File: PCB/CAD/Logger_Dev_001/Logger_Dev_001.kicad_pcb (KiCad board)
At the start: 2 copper layers, 72 parts, among them J1 Conn_Coaxial, J3 Micro_SD_Card_Det1, J4 Connector, USB-TYPE-C-16P, Q1 BC847BS, Q2 MMBT3904, U1 L76-M33, U2 ESP32-C6-WROOM-1, U5 AMS1117, U6 CP2102-GMR

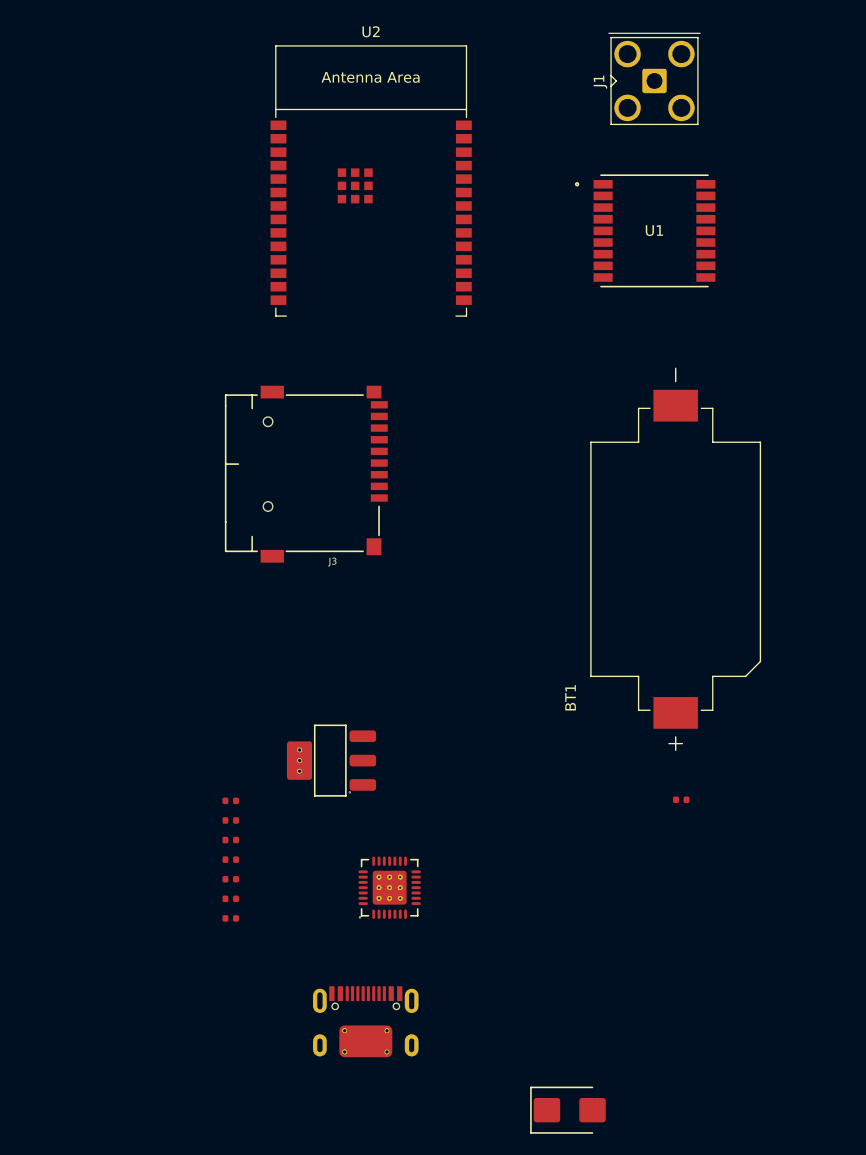
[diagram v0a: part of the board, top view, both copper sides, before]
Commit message: Update PCB
Added board outline, currently not showing in 3d viewer
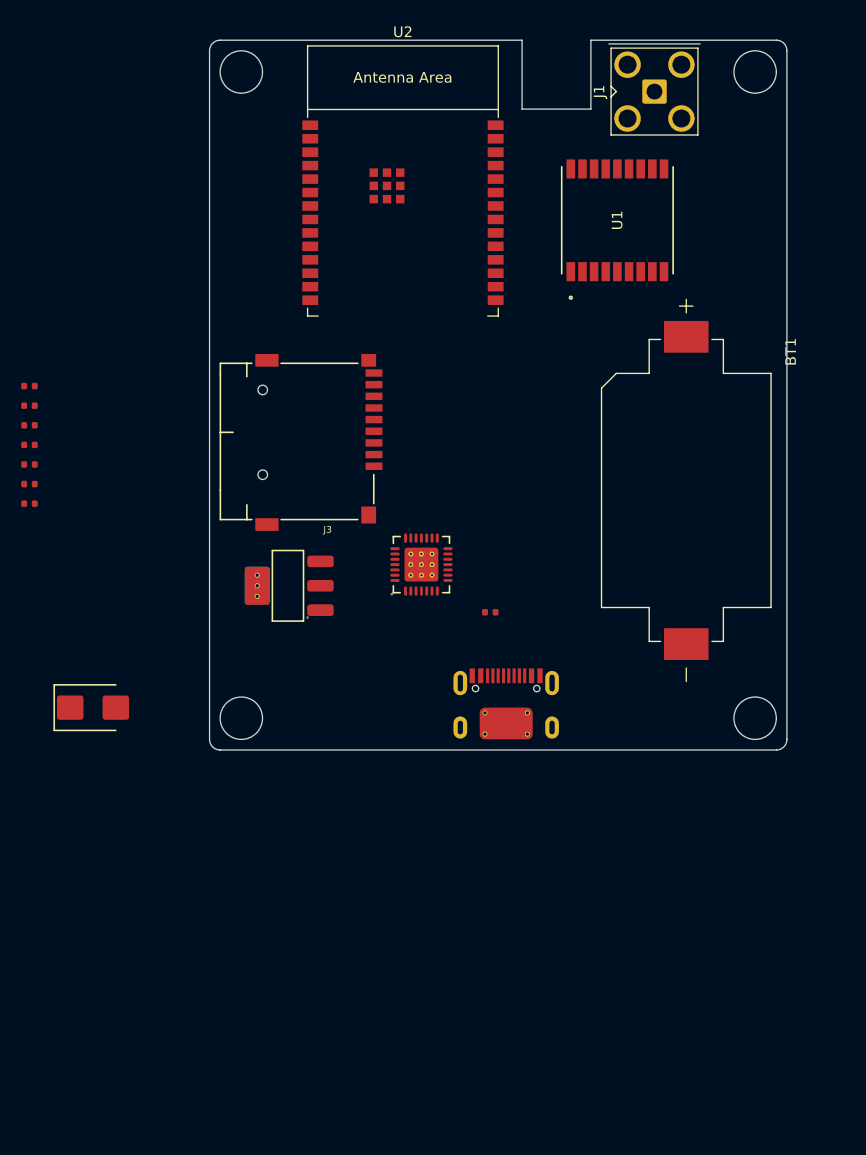
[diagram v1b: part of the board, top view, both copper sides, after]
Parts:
- moved D4 58.9 mm to (99.0, 107.0)
- moved C15 43.5 mm to (93.0, 78.5)
- moved R17 43.5 mm to (93.0, 80.3)
- moved R19 43.5 mm to (93.0, 84.0)
- moved R21 43.5 mm to (93.0, 87.8)
- moved C14 43.5 mm to (93.0, 76.7)
- moved R18 43.5 mm to (93.0, 82.2)
- moved R20 43.5 mm to (93.0, 85.9)
- moved J4 32.8 mm to (138.0, 106.5)
- moved U6 30.6 mm to (130.0, 93.5)
- moved C5 25.3 mm to (136.5, 98.0)
- moved U5 17.0 mm to (117.5, 95.5)
- moved BT1 6.58 mm to (155.0, 86.5), turned to -90 degrees
- moved U1 3.64 mm to (148.5, 61.0), turned to 90 degrees
- moved J3 3.04 mm to (118.5, 81.0)
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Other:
- board outline added: 54.5 x 67 mm

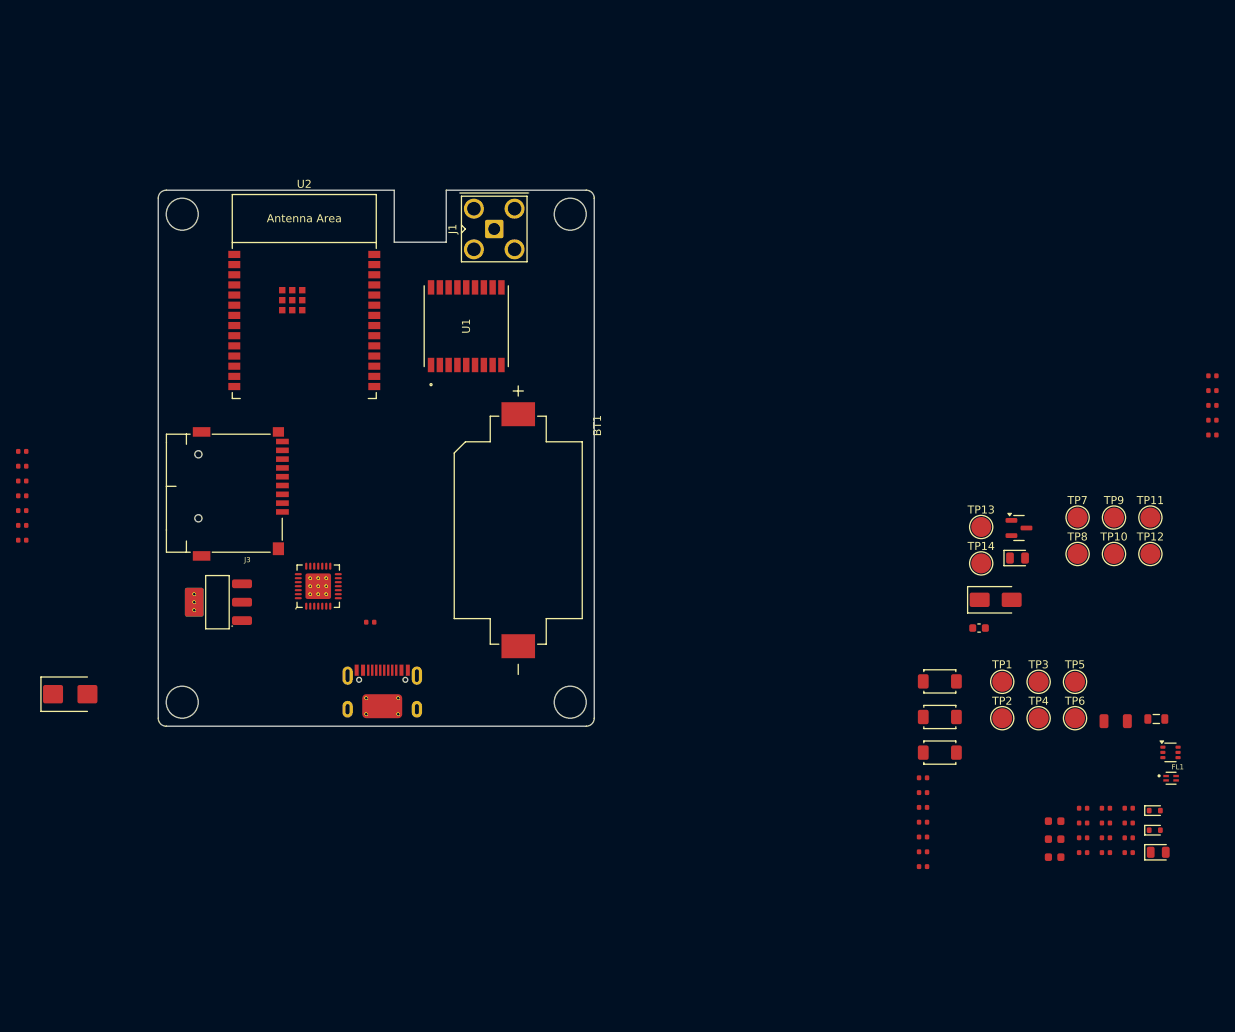
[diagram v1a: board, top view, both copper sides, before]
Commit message: PCB Board Update
Moved drill holes but board is broken by rf connector
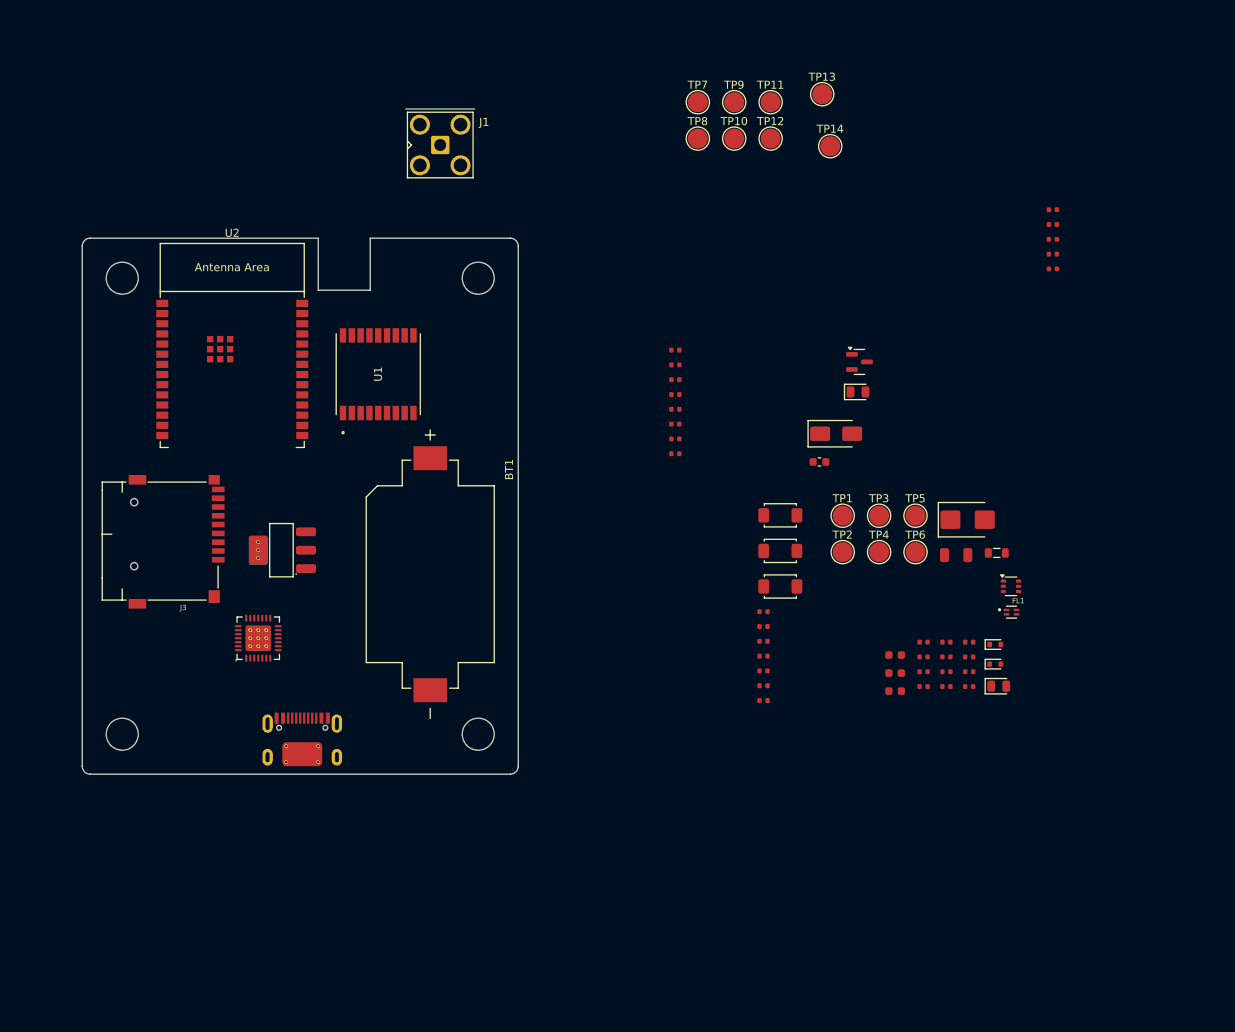
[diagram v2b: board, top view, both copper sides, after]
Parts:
- moved D4 114.3 mm to (211.2, 85.2)
- moved C14 82.4 mm to (174.6, 65.8)
- moved C15 82.4 mm to (174.6, 67.7)
- moved R17 82.4 mm to (174.6, 69.5)
- moved R18 82.4 mm to (174.6, 71.4)
- moved R19 82.4 mm to (174.6, 73.2)
- moved R20 82.4 mm to (174.6, 75.1)
- moved R21 82.4 mm to (174.6, 76.9)
- moved TP10 70.3 mm to (182.0, 37.5)
- moved TP11 70.3 mm to (186.6, 33.0)
- moved TP12 70.3 mm to (186.6, 37.5)
- moved TP7 70.3 mm to (177.4, 33.0)
- moved TP8 70.3 mm to (177.4, 37.5)
- moved TP9 70.3 mm to (182.0, 33.0)
- moved TP13 57.6 mm to (193.0, 32.0)
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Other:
- outline, holes or cut-outs redrawn

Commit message: PCB Layout Update
PCB Board Fixed
Most Components except Resistors placed
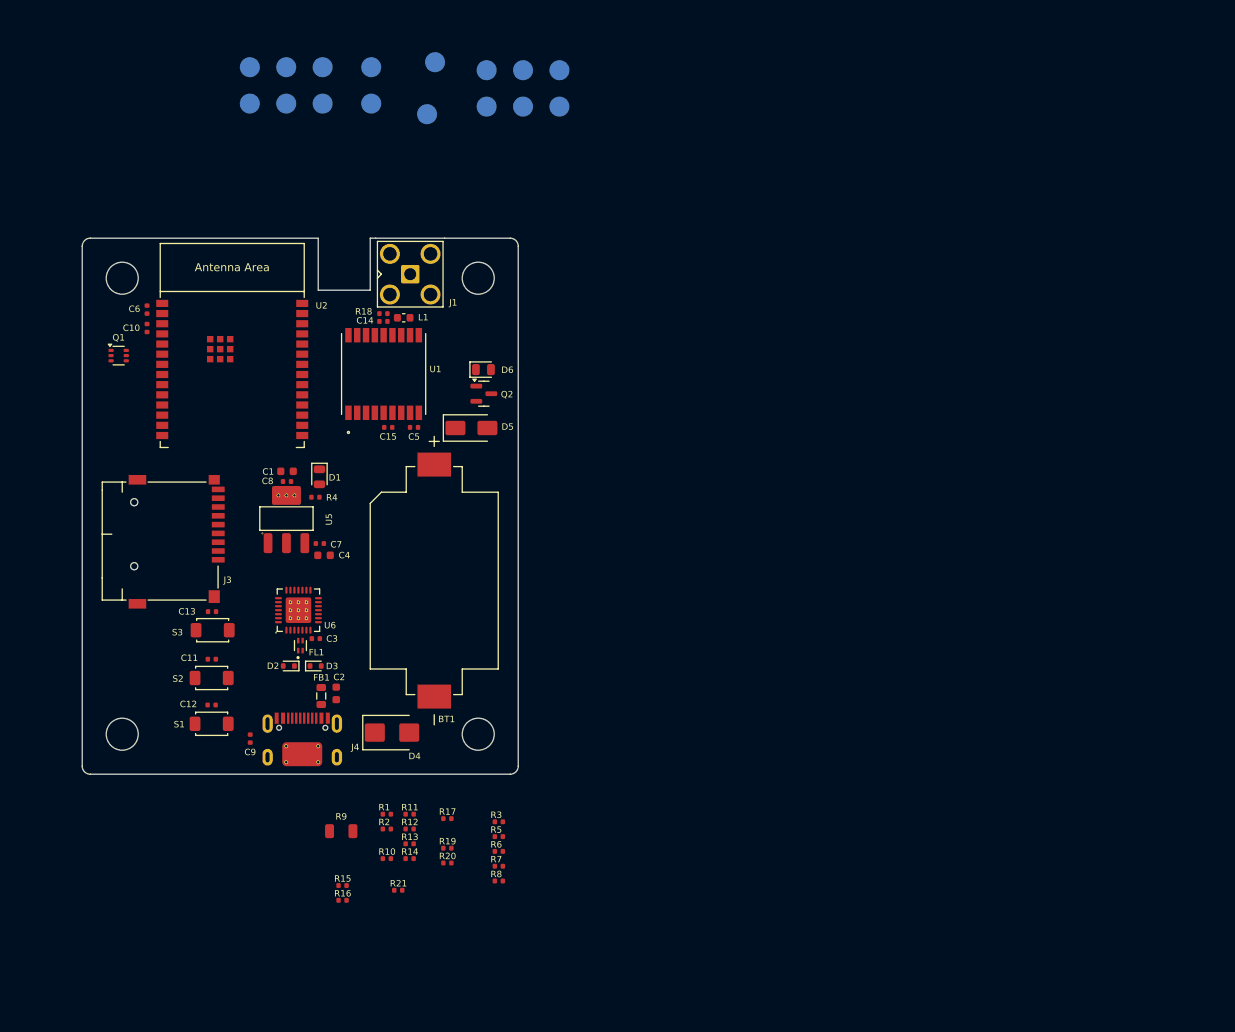
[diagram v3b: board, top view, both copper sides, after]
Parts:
- added TP15: FUNC_BTN_TP, TestPoint:TestPoint_Pad_D2.5mm, B.Cu at (136.6, 28.6)
- added TP16: GND_TP, TestPoint:TestPoint_Pad_D2.5mm, B.Cu at (136.6, 33.2)
- TP1, TP10, TP11, TP12, TP13, TP14, TP2, TP3, TP4, TP5, TP6, TP7, TP8, TP9: moved to B.Cu
- moved Q1 115.2 mm to (105.0, 64.7)
- moved R3 103.2 mm to (152.6, 123.0)
- moved R6 103.2 mm to (152.6, 126.7)
- moved R5 103.2 mm to (152.6, 124.8)
- moved R7 103.2 mm to (152.6, 128.5)
- moved R8 103.2 mm to (152.6, 130.3)
- moved TP5 100.3 mm to (121.5, 28.6), turned to 180 degrees
- moved TP6 100.3 mm to (121.5, 33.2), turned to 180 degrees
- moved TP3 92.9 mm to (126.0, 28.6), turned to 180 degrees
- moved TP4 92.9 mm to (126.0, 33.2), turned to 180 degrees
- moved FL1 89.0 mm to (127.8, 100.9), turned to 90 degrees
- moved D1 88.9 mm to (130.2, 79.8), turned to -90 degrees
- moved D2 88.3 mm to (126.3, 103.5), turned to 180 degrees
- moved FB1 86.3 mm to (130.4, 107.2), turned to -90 degrees
- moved TP1 85.8 mm to (130.6, 28.6), turned to 180 degrees
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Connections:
- D4 pad 1: Net-(D4-Pad1) -> VUSB
- FB1 pad 2: Net-(D4-Pad1) -> VUSB_UNFILTERD
- J4 pad A9B4: Net-(D4-Pad1) -> VUSB_UNFILTERD
- J4 pad B9A4: Net-(D4-Pad1) -> VUSB_UNFILTERD
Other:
- outline, holes or cut-outs redrawn

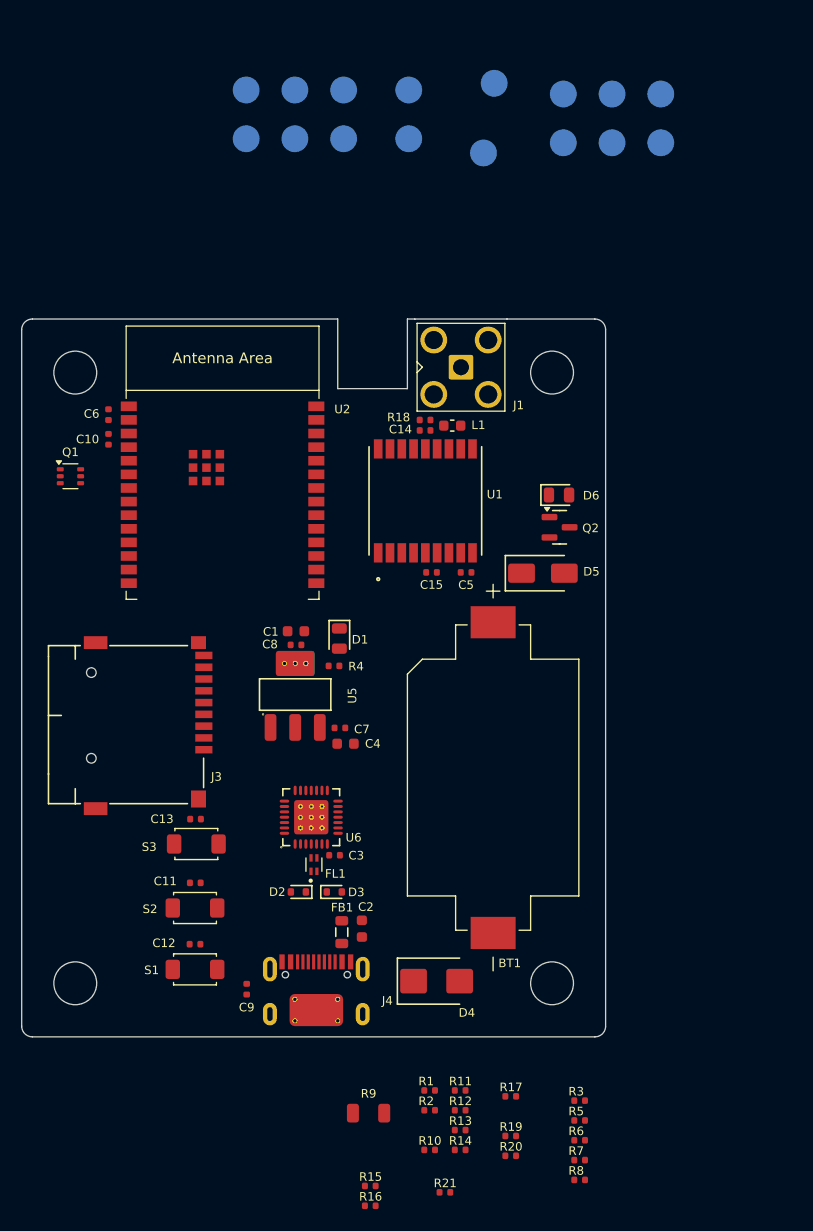
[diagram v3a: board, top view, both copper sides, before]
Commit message: PCB Board Update
Preliminary Components Placement.
Still to place all test points
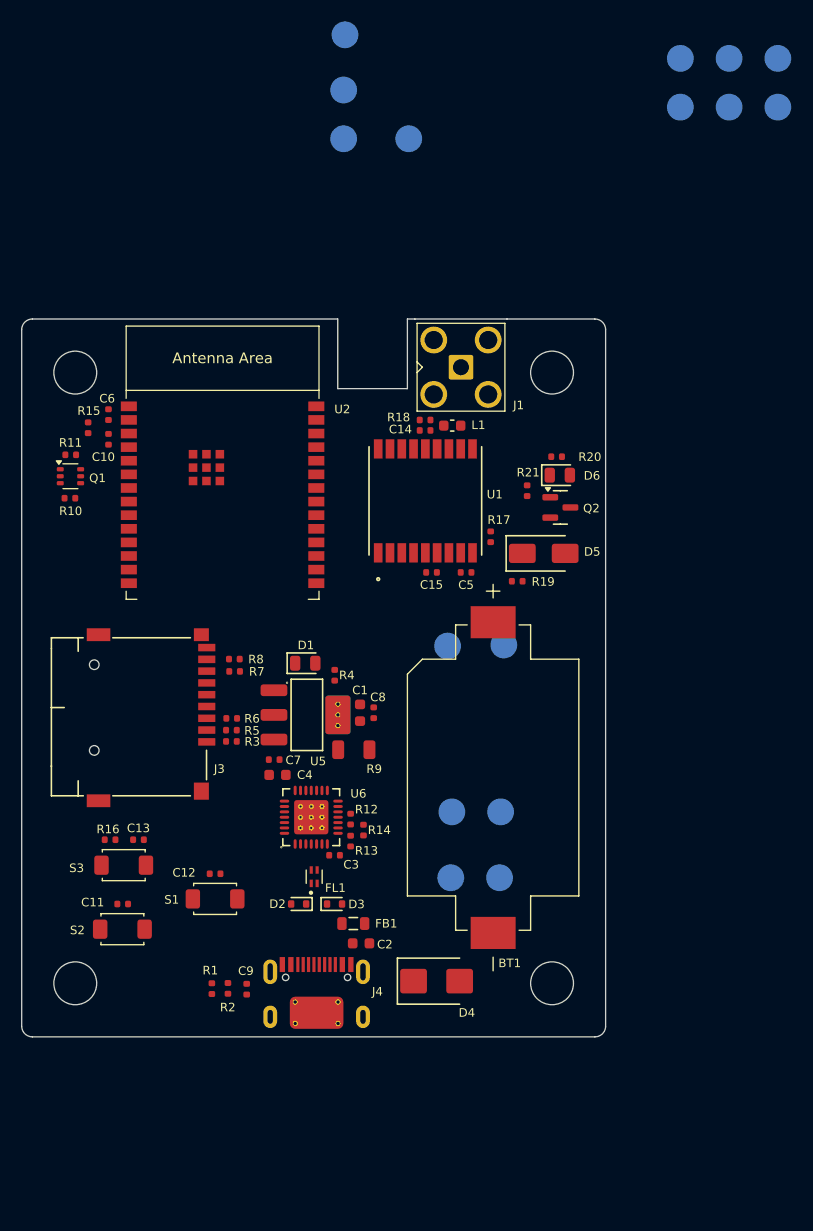
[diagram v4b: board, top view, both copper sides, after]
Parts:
- moved TP5 77.2 mm to (145.1, 102.2), turned to 90 degrees
- moved R15 75.5 mm to (106.7, 60.1), turned to -90 degrees
- moved TP6 71.6 mm to (140.6, 102.2), turned to 90 degrees
- moved TP3 70.1 mm to (145.2, 96.0), turned to 90 degrees
- moved R11 69.6 mm to (105.1, 62.7)
- moved R10 69.5 mm to (105.0, 66.7), turned to 180 degrees
- moved R21 65.9 mm to (147.7, 66.0), turned to -90 degrees
- moved R20 65.4 mm to (150.4, 62.9)
- moved TP4 64.5 mm to (140.7, 96.0), turned to 90 degrees
- moved R8 58.3 mm to (120.3, 81.7), turned to 180 degrees
- moved R7 55.8 mm to (120.4, 82.9), turned to 180 degrees
- moved TP13 52.4 mm to (145.5, 80.4)
- moved R17 52.3 mm to (144.3, 70.3), turned to -90 degrees
- moved R19 51.8 mm to (146.8, 74.5), turned to 180 degrees
- moved R6 51.0 mm to (120.1, 87.3), turned to 180 degrees
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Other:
- board text added: "GPS TX, RX"
- board text added: "UART TX, RX"
- board text added: "USB D+, D-"
